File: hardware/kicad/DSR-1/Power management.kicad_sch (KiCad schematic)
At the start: 0 parts

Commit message: Refactor code structure for improved readability and maintainability
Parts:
- added C10, C9: 1uF, symbol Device:C_US
- added C5, C6, C7: 10uf, symbol Device:C_US
- added C8: 47uF 16V, symbol Device:C_US
- added D7: SS14, Diode_SMD:D_SMA, symbol Diode:SS14
- added L2: 4.7uH, symbol Device:L
- added R3: 169k, symbol Device:R
- added R4: 10k, symbol Device:R
- added U2: MT3608, Package_TO_SOT_SMD:SOT-23-6, symbol DSR-1:MT3608
- added U4: MCP1700x-330xxTT, Package_TO_SOT_SMD:SOT-23, symbol DSR-1:MCP1700x-330xxTT
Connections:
- net +3.3V: now also C7.1, U4.2 (VO)
- net B+1: now also C5.1, C6.1, R3.1, U2.4 (EN), U2.5 (IN), U4.3 (VI)
- net B+3: now also C8.1, D7.2 (A)
- net GND: now also C10.2, C5.2, C8.2, C9.2, R4.2, U2.2 (GND), U4.1 (GND)
- new net: C6.2, C9.1
- new net: R3.2, R4.1, U2.3 (FB)
- new net: D7.1 (K), L2.2
- new net: L2.1, U2.1 (SW)
- new net: C10.1, C7.2
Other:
- note added: "B+3 output = 0.6 × (1 + 169k/10k) = 10.74V nominal. ⚠ SW NODE: high dV/dt at 1.2MHz. Keep SW trace <3mm. Minimum 2mm clearance to FG, ADC, and motor drive signal traces. C8 must be 47µF (not 22µF) - X5R derating at 10.8V reduces effective capacitance. Use 16V rated part for adequate margin."
- note added: "BRING-UP ORDER: 1. Verify 9V_PD present before AP63203 powers up 2. Check B+1 = 6.0-6.2V before enabling downstream 3. Check B+3 = 10.5-11V (no load) 4. Check +3.3V = 3.3V ±2% 5. Do not connect WM-D6C harness until all rails verified"
- note added: "Fixed 3.3V LDO. VIN max 16V - B+1 = 6V nominal, margin adequate. Requires minimum 1µF on VOUT for stability - C7+C10 exceed this."

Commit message: Completed microcontroller schematic
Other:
- title: (none) -> Power Management
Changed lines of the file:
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@@
 	(generator_version "10.0")
 	(paper "A4")
+	(title_block
+		(title "Power Management")
+		(date "2026-05-31")
+		(rev "1")
+	)
 	(text "Fixed 3.3V LDO. VIN max 16V - B+1 = 6V nominal, margin adequate.\nRequires minimum 1µF on VOUT for stability - C7+C10 exceed this."
 		(exclude_from_sim no)

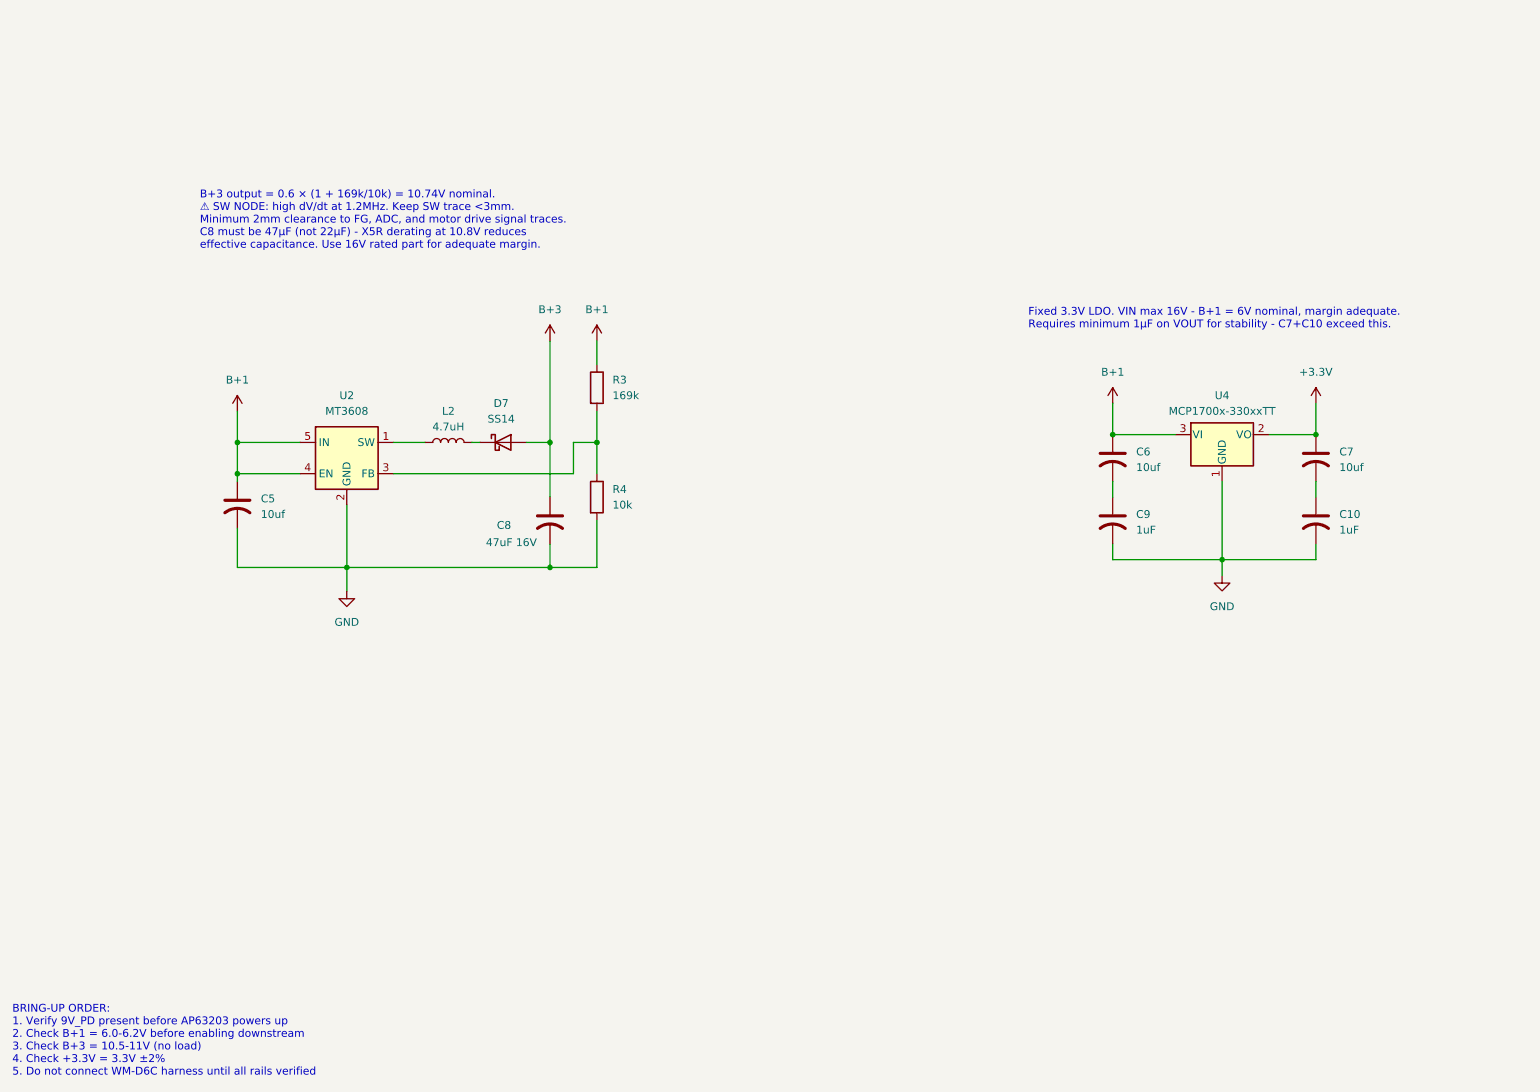
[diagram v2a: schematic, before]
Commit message: Update position of BRING-UP ORDER text in Power management schematic for better visibility
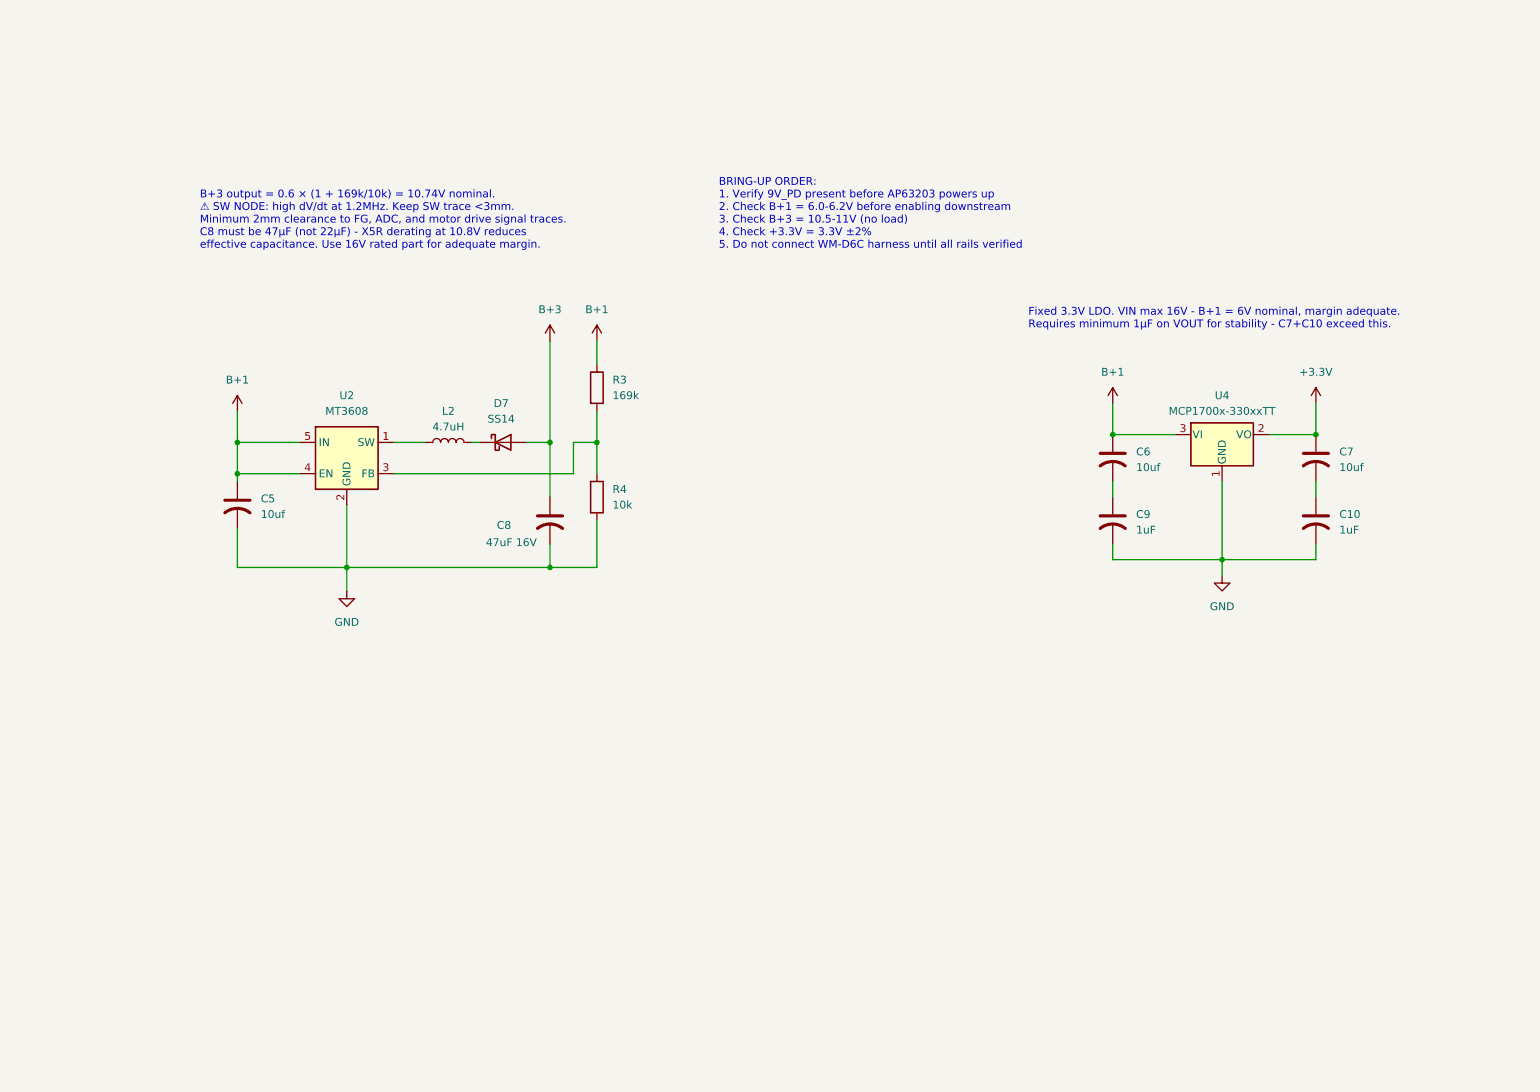
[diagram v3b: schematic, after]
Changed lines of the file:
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@@
 	(text "BRING-UP ORDER:\n1. Verify 9V_PD present before AP63203 powers up\n2. Check B+1 = 6.0-6.2V before enabling downstream\n3. Check B+3 = 10.5-11V (no load)\n4. Check +3.3V = 3.3V ±2%\n5. Do not connect WM-D6C harness until all rails verified"
 		(exclude_from_sim no)
-		(at 20.574 183.642 0)
+		(at 135.382 49.276 0)
 		(effects
 			(font
